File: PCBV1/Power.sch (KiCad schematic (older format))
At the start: 23 parts

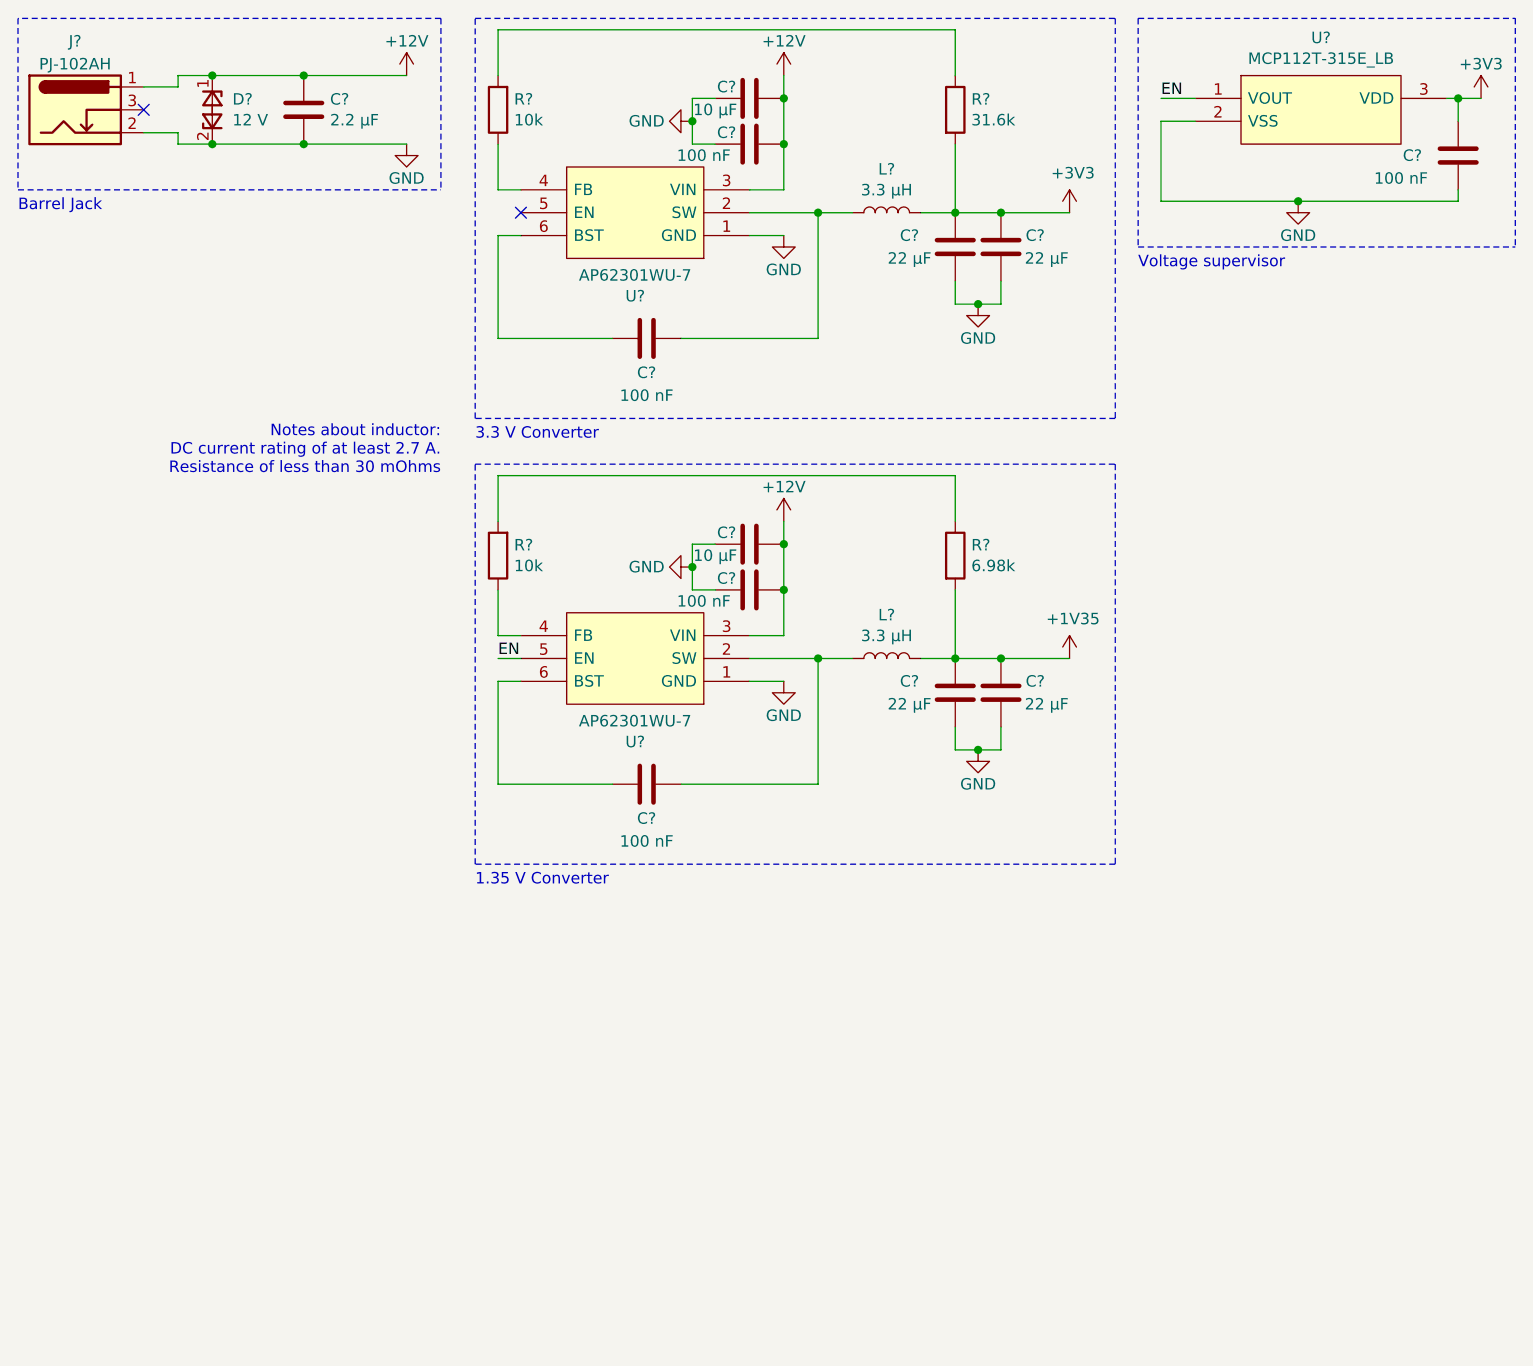
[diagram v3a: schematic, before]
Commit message: Many minor changes to component footprints and schematics.
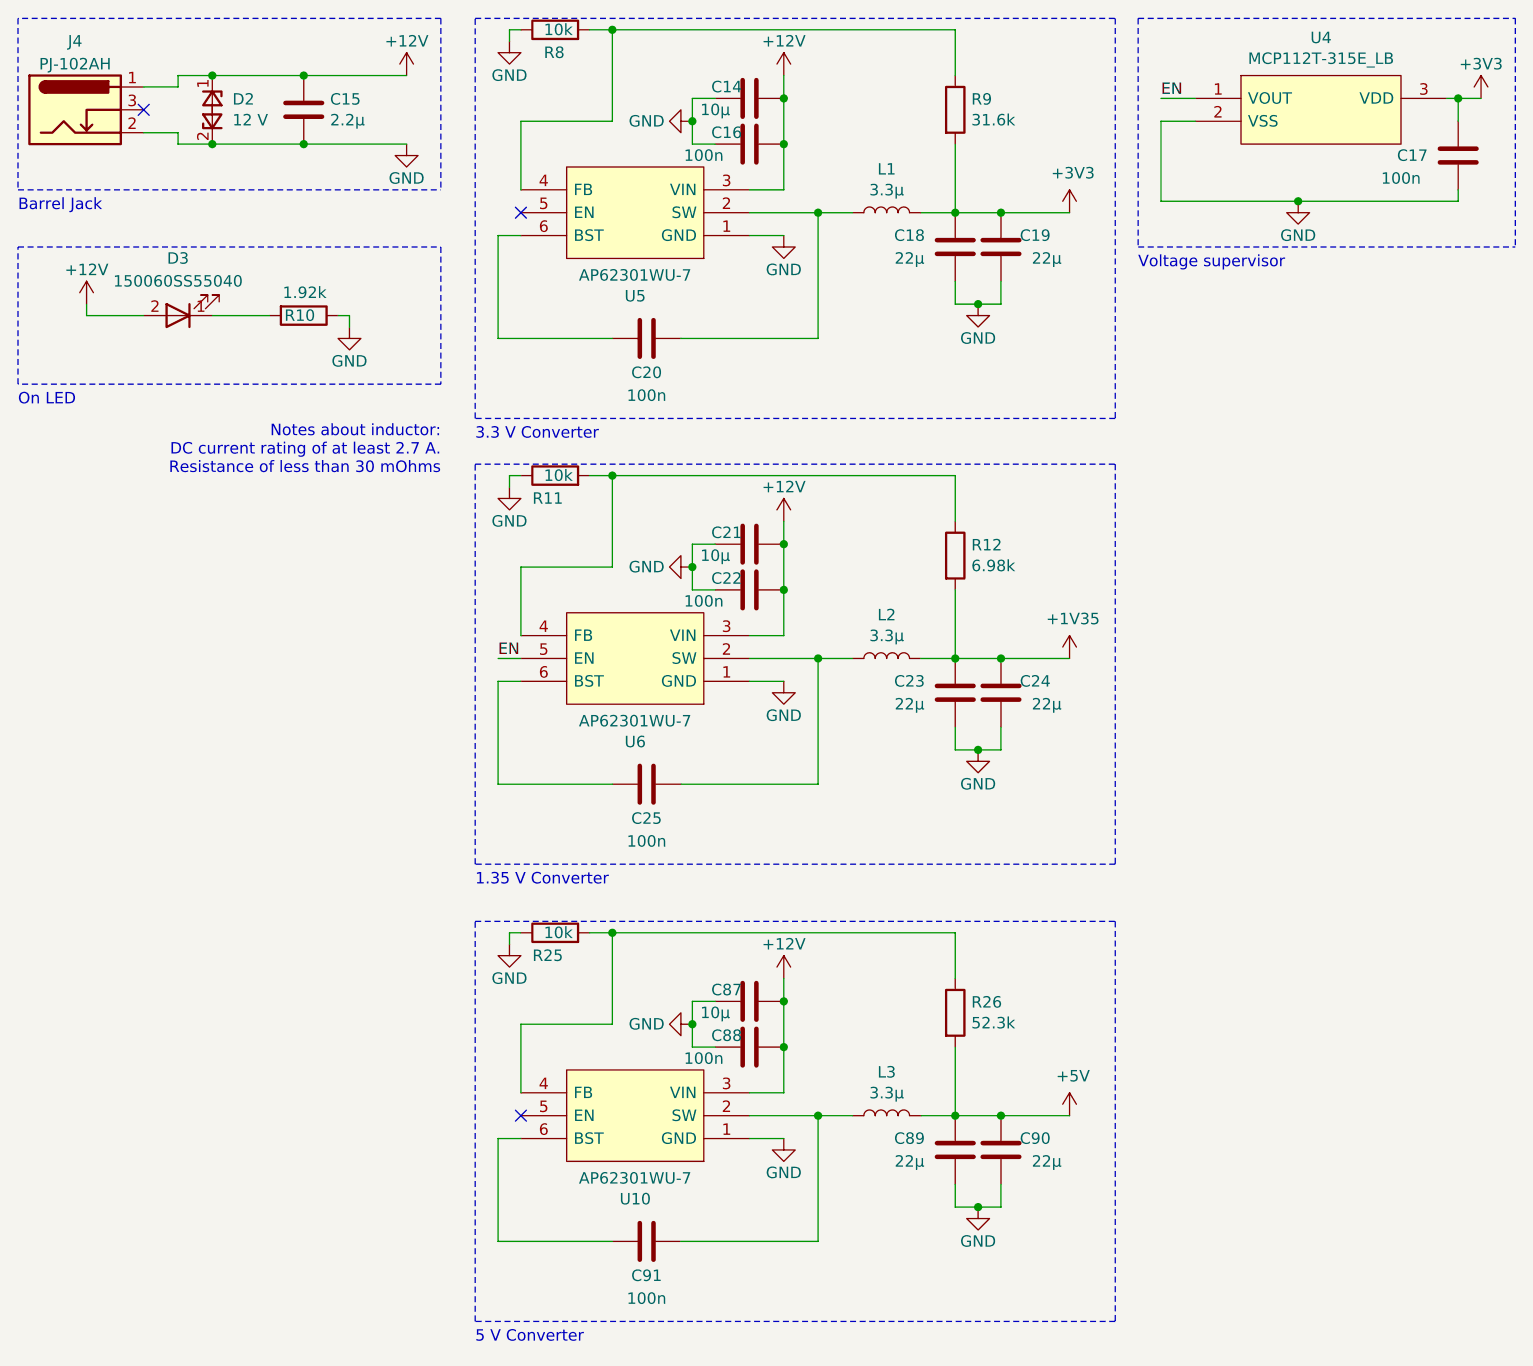
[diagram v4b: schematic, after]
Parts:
- added C87: 10µ, symbol Device:C
- added C88, C91: 100n, Capacitor_SMD:C_0603_1608Metric, symbol Device:C
- added C89, C90: 22µ, symbol Device:C
- added D3: 150060SS55040, Personal_Passives:150060SS55040, symbol Personal_Passives:150060SS55040
- added L3: 3.3µ, symbol Device:L
- added R10: 1.92k, Resistor_SMD:R_0603_1608Metric, symbol Device:R
- added R25: 10k, Resistor_SMD:R_0603_1608Metric, symbol Device:R
- added R26: 52.3k, Resistor_SMD:R_0603_1608Metric, symbol Device:R
- added U10: AP62301WU-7, Personal_ICs:AP62301WU-7, symbol Personal_ICs:AP62301WU-7
- C14, C21: renamed from C?; value 10 µF -> 10µ
- C15: renamed from C?; value 2.2 µF -> 2.2µ
- C16, C17, C20, C22, C25: renamed from C?; value 100 nF -> 100n; footprint (none) -> Capacitor_SMD:C_0603_1608Metric
- C18, C19, C23, C24: renamed from C?; value 22 µF -> 22µ
- J4: renamed from J?; footprint Connector_BarrelJack:BarrelJack_CUI_PJ-102AH_Horizontal -> Personal_Misc:BarrelJack_CUI_PJ-102AH_Horizontal
- L1, L2: renamed from L?; value 3.3 µH -> 3.3µ
- R11, R12, R8, R9: renamed from R?; footprint (none) -> Resistor_SMD:R_0603_1608Metric
- gave numbers to parts that had none: 4
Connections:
- net +12V: now also C87.2, C88.2, D3.2 (A), U10.3 (VIN)
- net GND: now also R11.1, R8.1, C87.1, C88.1, C89.2, C90.2, R10.1, R25.1, U10.1 (GND)
- net at U5.4 (FB): now also R8.2, R9.1; no longer R8.1
- net at U6.4 (FB): now also R11.2, R12.1; no longer R11.1
- new net: C91.2, L3.1, U10.2 (SW)
- new net: R25.2, R26.1, U10.4 (FB)
- new net: C91.1, U10.6 (BST)
- new net: D3.1 (K), R10.2
- new net +5V: C89.1, C90.1, L3.2, R26.2
- no-connect marks 2 -> 3
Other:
- note added: "5 V Converter"
- note added: "On LED"
- moved on the sheet: R11, R8

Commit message: Added NAND flash with connections, updated IO config.
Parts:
- C18, C19, C23, C24, C89, C90: footprint (none) -> Capacitor_SMD:C_0603_1608Metric
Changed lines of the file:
@@
 F 0 "C18" H 4900 2050 50  0000 C CNN
 F 1 "22µ" H 4900 1950 50  0000 C CNN
-F 2 "" H 5138 1850 50  0001 C CNN
+F 2 "Capacitor_SMD:C_0603_1608Metric" H 5138 1850 50  0001 C CNN
 F 3 "~" H 5100 2000 50  0001 C CNN
 	1    5100 2000
@@
 F 0 "C19" H 5450 2050 50  0000 C CNN
 F 1 "22µ" H 5500 1950 50  0000 C CNN
-F 2 "" H 5338 1850 50  0001 C CNN
+F 2 "Capacitor_SMD:C_0603_1608Metric" H 5338 1850 50  0001 C CNN
 F 3 "~" H 5300 2000 50  0001 C CNN
 	1    5300 2000
@@
 F 0 "C23" H 4900 4000 50  0000 C CNN
 F 1 "22µ" H 4900 3900 50  0000 C CNN
-F 2 "" H 5138 3800 50  0001 C CNN
+F 2 "Capacitor_SMD:C_0603_1608Metric" H 5138 3800 50  0001 C CNN
 F 3 "~" H 5100 3950 50  0001 C CNN
 	1    5100 3950
@@
 F 0 "C24" H 5450 4000 50  0000 C CNN
 F 1 "22µ" H 5500 3900 50  0000 C CNN
-F 2 "" H 5338 3800 50  0001 C CNN
+F 2 "Capacitor_SMD:C_0603_1608Metric" H 5338 3800 50  0001 C CNN
 F 3 "~" H 5300 3950 50  0001 C CNN
 	1    5300 3950
@@
 F 0 "C89" H 4900 6000 50  0000 C CNN
 F 1 "22µ" H 4900 5900 50  0000 C CNN
-F 2 "" H 5138 5800 50  0001 C CNN
+F 2 "Capacitor_SMD:C_0603_1608Metric" H 5138 5800 50  0001 C CNN
 F 3 "~" H 5100 5950 50  0001 C CNN
 	1    5100 5950
@@
 F 0 "C90" H 5450 6000 50  0000 C CNN
 F 1 "22µ" H 5500 5900 50  0000 C CNN
-F 2 "" H 5338 5800 50  0001 C CNN
+F 2 "Capacitor_SMD:C_0603_1608Metric" H 5338 5800 50  0001 C CNN
 F 3 "~" H 5300 5950 50  0001 C CNN
 	1    5300 5950

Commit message: Laid final hands on Wi-Fi and all circuits. Started work on PCB.
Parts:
- removed L2, L3: 3.3µ, symbol Device:L
- added L4, L5: 3.3µ, Inductor_SMD:L_Taiyo-Yuden_NR-80xx, symbol Device:L
- C34: renamed from C14; footprint (none) -> Capacitor_SMD:C_0805_2012Metric
- C41: renamed from C21; footprint (none) -> Capacitor_SMD:C_0805_2012Metric
- C46: renamed from C87; footprint (none) -> Capacitor_SMD:C_0805_2012Metric
- L3: renamed from L1; footprint (none) -> Inductor_SMD:L_Taiyo-Yuden_NR-80xx; Name (none) -> NRS8030T3R3MJGJ
- renumbered C15 to C35, C16 to C36, C17 to C37, C18 to C38, C19 to C39, C20 to C40, C22 to C42, C23 to C43, C24 to C44, C25 to C45, C88 to C47, C89 to C48, C90 to C49, C91 to C50, R8 to R20, R9 to R21, R10 to R22, R11 to R23, R12 to R24, U5 to U10, U6 to U11, U10 to U12, U4 to U9
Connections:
- net +1V35: now also L4.2
- net +5V: now also L5.2
- net at C45.2, U11.2 (SW): now also L4.1
- net at C50.2, U12.2 (SW): now also L5.1

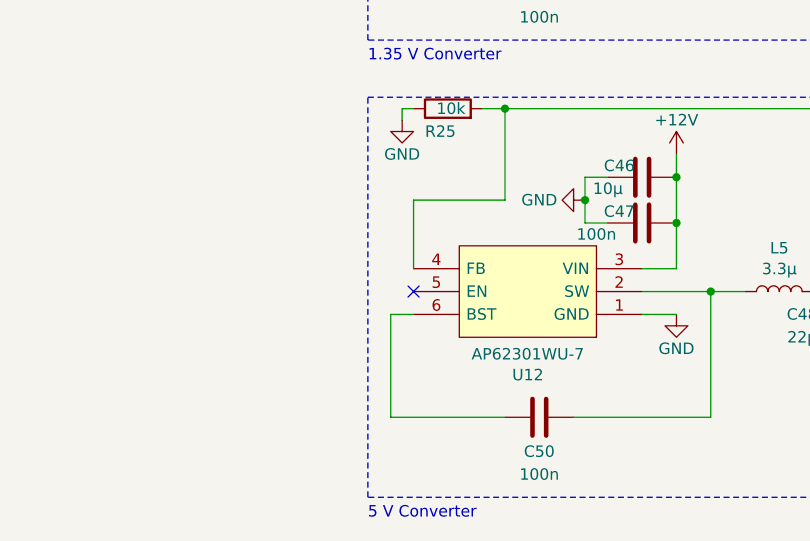
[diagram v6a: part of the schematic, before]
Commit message: Added JTAG, USB OTG, USB Host, and Ethernet.
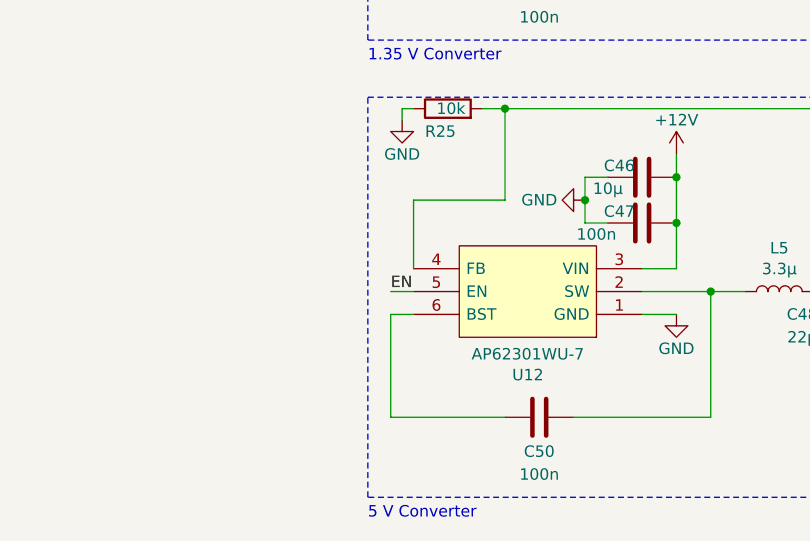
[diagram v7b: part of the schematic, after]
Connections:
- net EN: now also U12.5 (EN)
- no-connect marks 3 -> 2
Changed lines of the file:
@@
 $Descr A4 11693 8268
 encoding utf-8
-Sheet 5 8
+Sheet 5 11
 Title "Smart Mirror"
 Date "2022-05-11"
@@
 	1    0    0    -1
 $EndComp
-NoConn ~ 3200 5800
 $Comp
 L Device:L L4
@@
 	0    -1   -1   0
 $EndComp
+Text Label 3100 5800 0    50   ~ 0
+EN
+Wire Wire Line
+	3200 5800 3100 5800
 $EndSCHEMATC
